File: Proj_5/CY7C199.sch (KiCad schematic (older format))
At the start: 8 parts

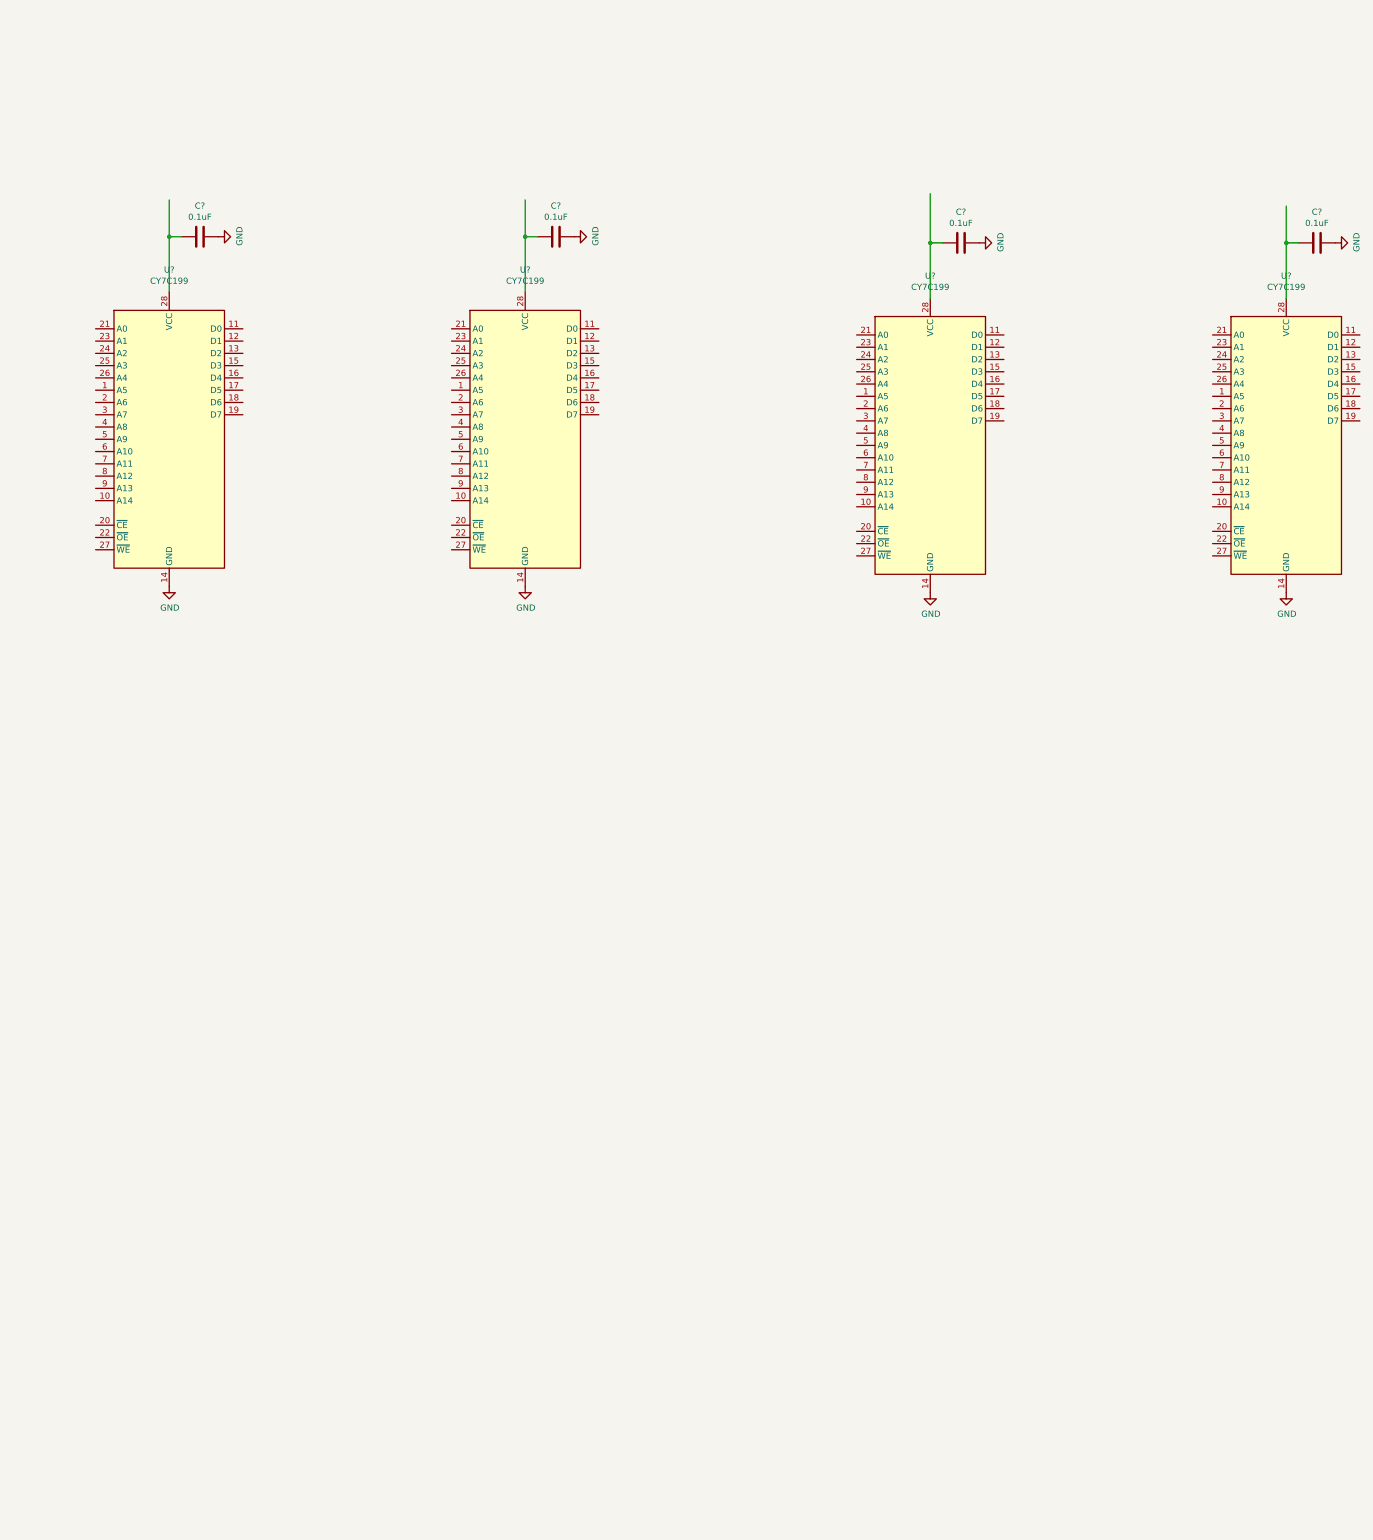
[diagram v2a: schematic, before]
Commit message: Changed Addressing Again
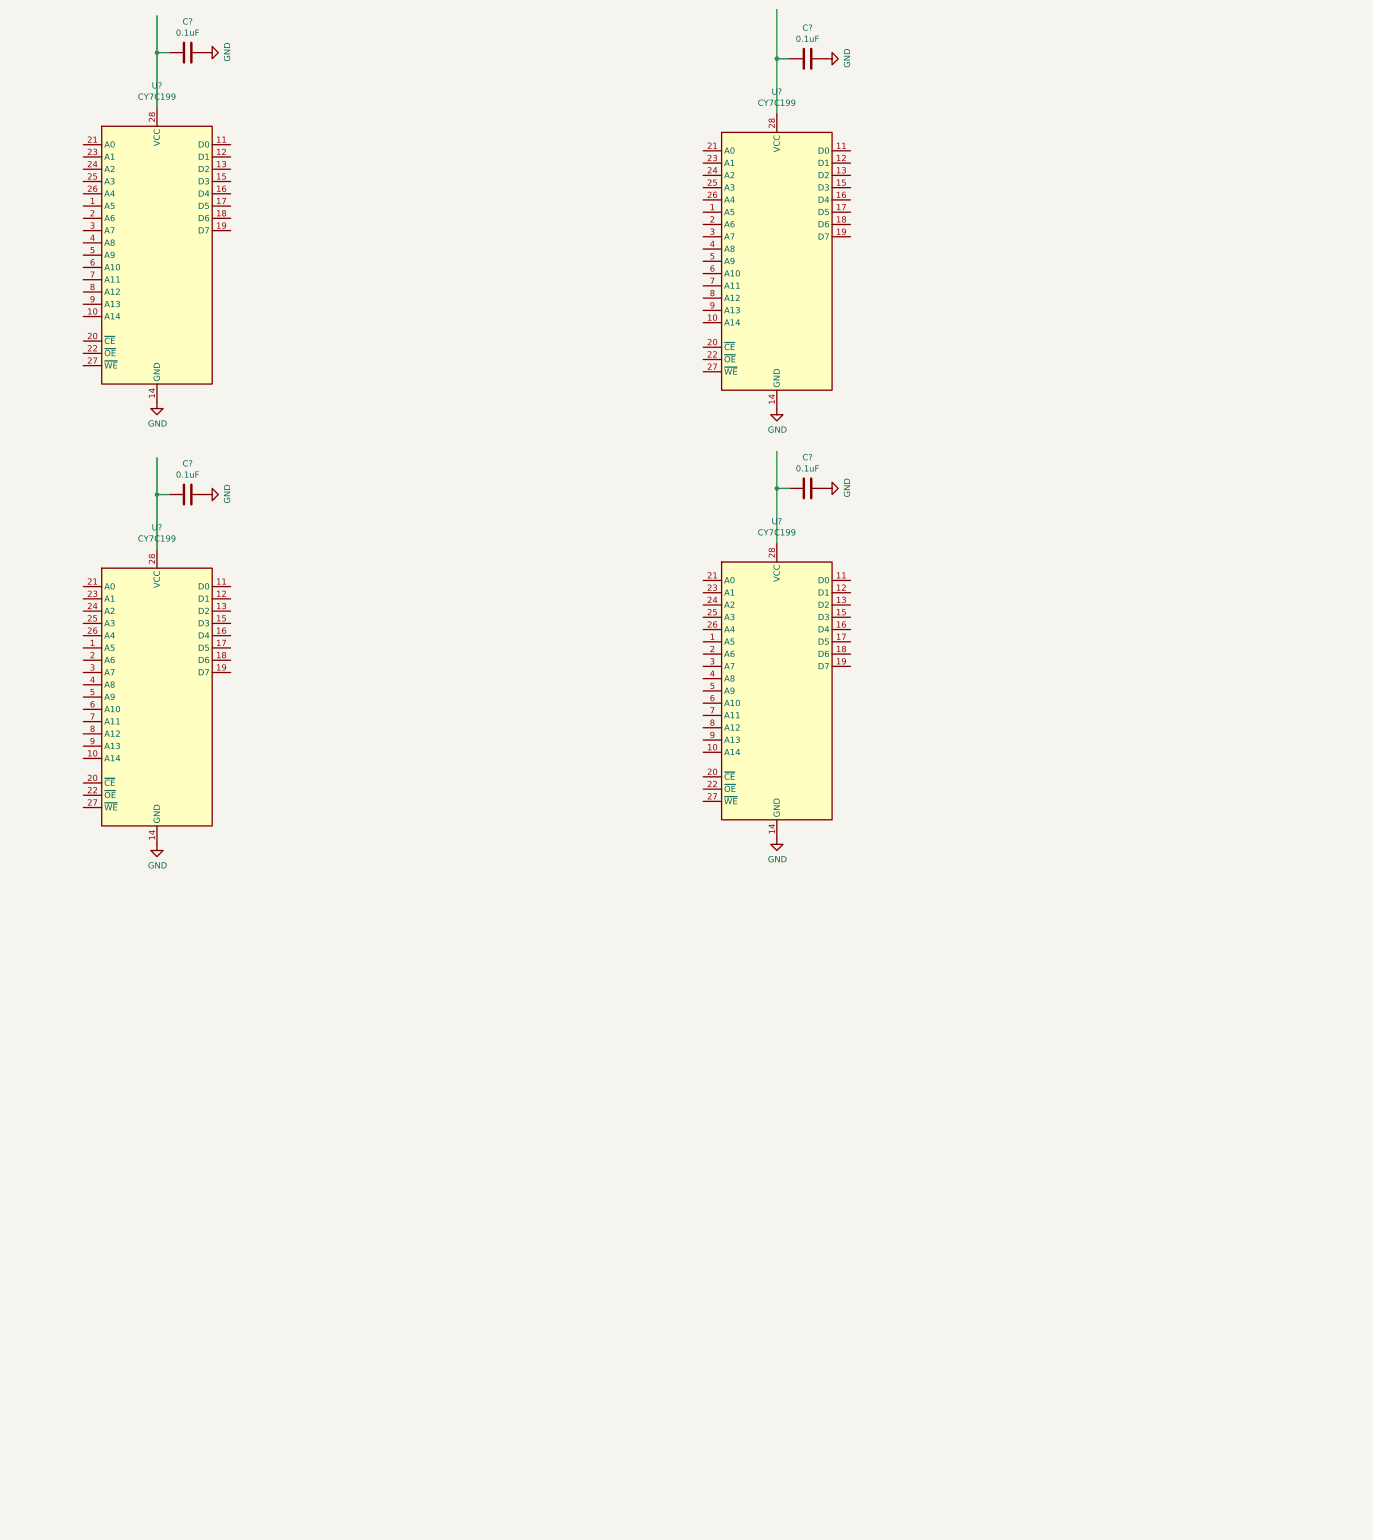
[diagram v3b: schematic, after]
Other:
- moved on the sheet: C?, U?
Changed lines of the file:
@@
 L Memory_RAM:CY7C199 U?
 U 1 1 5EA4313E
-P 4650 4500
-F 0 "U?" H 4650 5881 50  0000 C CNN
-F 1 "CY7C199" H 4650 5790 50  0000 C CNN
-F 2 "" H 4650 4500 50  0001 C CNN
-F 3 "" H 4650 4500 50  0001 C CNN
-	1    4650 4500
+P 4550 3000
+F 0 "U?" H 4550 4381 50  0000 C CNN
+F 1 "CY7C199" H 4550 4290 50  0000 C CNN
+F 2 "" H 4550 3000 50  0001 C CNN
+F 3 "" H 4550 3000 50  0001 C CNN
+	1    4550 3000
 	1    0    0    -1
 $EndComp
@@
 L Memory_RAM:CY7C199 U?
 U 1 1 5EA4B54C
-P 7550 4500
-F 0 "U?" H 7550 5881 50  0000 C CNN
-F 1 "CY7C199" H 7550 5790 50  0000 C CNN
-F 2 "" H 7550 4500 50  0001 C CNN
-F 3 "" H 7550 4500 50  0001 C CNN
-	1    7550 4500
+P 4550 6600
+F 0 "U?" H 4550 7981 50  0000 C CNN
+F 1 "CY7C199" H 4550 7890 50  0000 C CNN
+F 2 "" H 4550 6600 50  0001 C CNN
+F 3 "" H 4550 6600 50  0001 C CNN
+	1    4550 6600
 	1    0    0    -1
 $EndComp
@@
 L Memory_RAM:CY7C199 U?
 U 1 1 5EA4FA2E
-P 10850 4550
-F 0 "U?" H 10850 5931 50  0000 C CNN
-F 1 "CY7C199" H 10850 5840 50  0000 C CNN
-F 2 "" H 10850 4550 50  0001 C CNN
-F 3 "" H 10850 4550 50  0001 C CNN
-	1    10850 4550
+P 9600 3050
+F 0 "U?" H 9600 4431 50  0000 C CNN
+F 1 "CY7C199" H 9600 4340 50  0000 C CNN
+F 2 "" H 9600 3050 50  0001 C CNN
+F 3 "" H 9600 3050 50  0001 C CNN
+	1    9600 3050
 	1    0    0    -1
 $EndComp
@@
 L Memory_RAM:CY7C199 U?
 U 1 1 5EA4FA34
-P 13750 4550
-F 0 "U?" H 13750 5931 50  0000 C CNN
-F 1 "CY7C199" H 13750 5840 50  0000 C CNN
-F 2 "" H 13750 4550 50  0001 C CNN
-F 3 "" H 13750 4550 50  0001 C CNN
-	1    13750 4550
+P 9600 6550
+F 0 "U?" H 9600 7931 50  0000 C CNN
+F 1 "CY7C199" H 9600 7840 50  0000 C CNN
+F 2 "" H 9600 6550 50  0001 C CNN
+F 3 "" H 9600 6550 50  0001 C CNN
+	1    9600 6550
 	1    0    0    -1
 $EndComp
@@
 L Device:C C?
 U 1 1 5EA524F8
-P 14000 2900
-F 0 "C?" V 13748 2900 50  0000 C CNN
-F 1 "0.1uF" V 13839 2900 50  0000 C CNN
-F 2 "" H 14038 2750 50  0001 C CNN
-F 3 "~" H 14000 2900 50  0001 C CNN
-	1    14000 2900
+P 9850 4900
+F 0 "C?" V 9598 4900 50  0000 C CNN
+F 1 "0.1uF" V 9689 4900 50  0000 C CNN
+F 2 "" H 9888 4750 50  0001 C CNN
+F 3 "~" H 9850 4900 50  0001 C CNN
+	1    9850 4900
 	0    1    1    0
 $EndComp
@@
 L Device:C C?
 U 1 1 5EA53D82
-P 11100 2900
-F 0 "C?" V 10848 2900 50  0000 C CNN
-F 1 "0.1uF" V 10939 2900 50  0000 C CNN
-F 2 "" H 11138 2750 50  0001 C CNN
-F 3 "~" H 11100 2900 50  0001 C CNN
-	1    11100 2900
-	0    1    1    0
-$EndComp
-Wire Wire Line
-	13850 2900 13750 2900
-Wire Wire Line
-	13750 2900 13750 3350
-Wire Wire Line
-	13750 2900 13750 2600
-Connection ~ 13750 2900
+P 9850 1400
+F 0 "C?" V 9598 1400 50  0000 C CNN
+F 1 "0.1uF" V 9689 1400 50  0000 C CNN
+F 2 "" H 9888 1250 50  0001 C CNN
+F 3 "~" H 9850 1400 50  0001 C CNN
+	1    9850 1400
+	0    1    1    0
+$EndComp
+Wire Wire Line
+	9700 4900 9600 4900
+Wire Wire Line
+	9600 4900 9600 5350
+Wire Wire Line
+	9600 4900 9600 4600
+Connection ~ 9600 4900
 $Comp
 L power:GND #PWR?
 U 1 1 5EAA219F
-P 14150 2900
+P 10000 4900
 AR Path="/5E9F3A3D/5EAA219F" Ref="#PWR?"  Part="1"
 AR Path="/5EA98353/5EAA219F" Ref="#PWR?"  Part="1"
-F 0 "#PWR?" H 14150 2650 50  0001 C CNN
-F 1 "GND" H 14155 2727 50  0000 C CNN
-F 2 "" H 14150 2900 50  0001 C CNN
-F 3 "" H 14150 2900 50  0001 C CNN
-	1    14150 2900
+F 0 "#PWR?" H 10000 4650 50  0001 C CNN
+F 1 "GND" H 10005 4727 50  0000 C CNN
+F 2 "" H 10000 4900 50  0001 C CNN
+F 3 "" H 10000 4900 50  0001 C CNN
+	1    10000 4900
 	0    -1   -1   0
 $EndComp
@@
 L power:GND #PWR?
 U 1 1 5EAA2618
-P 11250 2900
+P 10000 1400
 AR Path="/5E9F3A3D/5EAA2618" Ref="#PWR?"  Part="1"
 AR Path="/5EA98353/5EAA2618" Ref="#PWR?"  Part="1"
-F 0 "#PWR?" H 11250 2650 50  0001 C CNN
-F 1 "GND" H 11255 2727 50  0000 C CNN
-F 2 "" H 11250 2900 50  0001 C CNN
-F 3 "" H 11250 2900 50  0001 C CNN
-	1    11250 2900
-	0    -1   -1   0
-$EndComp
-Wire Wire Line
-	10950 2900 10850 2900
-Wire Wire Line
-	10850 2900 10850 3350
+F 0 "#PWR?" H 10000 1150 50  0001 C CNN
+F 1 "GND" H 10005 1227 50  0000 C CNN
+F 2 "" H 10000 1400 50  0001 C CNN
+F 3 "" H 10000 1400 50  0001 C CNN
+	1    10000 1400
+	0    -1   -1   0
+$EndComp
+Wire Wire Line
+	9700 1400 9600 1400
+Wire Wire Line
+	9600 1400 9600 1850
 $Comp
 L Device:C C?
 U 1 1 5EAB250B
-P 7800 2850
-F 0 "C?" V 7548 2850 50  0000 C CNN
-F 1 "0.1uF" V 7639 2850 50  0000 C CNN
-F 2 "" H 7838 2700 50  0001 C CNN
-F 3 "~" H 7800 2850 50  0001 C CNN
-	1    7800 2850
-	0    1    1    0
-$EndComp
-Wire Wire Line
-	7650 2850 7550 2850
-Wire Wire Line
-	7550 2850 7550 3300
-Wire Wire Line
-	7550 2850 7550 2550
-Connection ~ 7550 2850
+P 4800 4950
+F 0 "C?" V 4548 4950 50  0000 C CNN
+F 1 "0.1uF" V 4639 4950 50  0000 C CNN
+F 2 "" H 4838 4800 50  0001 C CNN
+F 3 "~" H 4800 4950 50  0001 C CNN
+	1    4800 4950
+	0    1    1    0
+$EndComp
+Wire Wire Line
+	4650 4950 4550 4950
+Wire Wire Line
+	4550 4950 4550 5400
+Wire Wire Line
+	4550 4950 4550 4650
+Connection ~ 4550 4950
 $Comp
 L power:GND #PWR?
 U 1 1 5EAB2515
-P 7950 2850
+P 4950 4950
 AR Path="/5E9F3A3D/5EAB2515" Ref="#PWR?"  Part="1"
 AR Path="/5EA98353/5EAB2515" Ref="#PWR?"  Part="1"
-F 0 "#PWR?" H 7950 2600 50  0001 C CNN
-F 1 "GND" H 7955 2677 50  0000 C CNN
-F 2 "" H 7950 2850 50  0001 C CNN
-F 3 "" H 7950 2850 50  0001 C CNN
-	1    7950 2850
+F 0 "#PWR?" H 4950 4700 50  0001 C CNN
+F 1 "GND" H 4955 4777 50  0000 C CNN
+F 2 "" H 4950 4950 50  0001 C CNN
+F 3 "" H 4950 4950 50  0001 C CNN
+	1    4950 4950
 	0    -1   -1   0
 $EndComp
@@
 L Device:C C?
 U 1 1 5EAB3F01
-P 4900 2850
-F 0 "C?" V 4648 2850 50  0000 C CNN
-F 1 "0.1uF" V 4739 2850 50  0000 C CNN
-F 2 "" H 4938 2700 50  0001 C CNN
-F 3 "~" H 4900 2850 50  0001 C CNN
-	1    4900 2850
-	0    1    1    0
-$EndComp
-Wire Wire Line
-	4750 2850 4650 2850
-Wire Wire Line
-	4650 2850 4650 3300
-Wire Wire Line
-	4650 2850 4650 2550
-Connection ~ 4650 2850
+P 4800 1350
+F 0 "C?" V 4548 1350 50  0000 C CNN
+F 1 "0.1uF" V 4639 1350 50  0000 C CNN
+F 2 "" H 4838 1200 50  0001 C CNN
+F 3 "~" H 4800 1350 50  0001 C CNN
+	1    4800 1350
+	0    1    1    0
+$EndComp
+Wire Wire Line
+	4650 1350 4550 1350
+Wire Wire Line
+	4550 1350 4550 1800
+Wire Wire Line
+	4550 1350 4550 1050
+Connection ~ 4550 1350
 $Comp
 L power:GND #PWR?
 U 1 1 5EAB3F0B
-P 5050 2850
+P 4950 1350
 AR Path="/5E9F3A3D/5EAB3F0B" Ref="#PWR?"  Part="1"
 AR Path="/5EA98353/5EAB3F0B" Ref="#PWR?"  Part="1"
-F 0 "#PWR?" H 5050 2600 50  0001 C CNN
-F 1 "GND" H 5055 2677 50  0000 C CNN
-F 2 "" H 5050 2850 50  0001 C CNN
-F 3 "" H 5050 2850 50  0001 C CNN
-	1    5050 2850
-	0    -1   -1   0
-$EndComp
-Wire Wire Line
-	10850 2900 10850 2500
-Connection ~ 10850 2900
+F 0 "#PWR?" H 4950 1100 50  0001 C CNN
+F 1 "GND" H 4955 1177 50  0000 C CNN
+F 2 "" H 4950 1350 50  0001 C CNN
+F 3 "" H 4950 1350 50  0001 C CNN
+	1    4950 1350
+	0    -1   -1   0
+$EndComp
+Wire Wire Line
+	9600 1400 9600 1000
+Connection ~ 9600 1400
 $Comp
 L power:GND #PWR?
 U 1 1 5EAB5C11
-P 10850 5750
+P 9600 4250
 AR Path="/5E9F3A3D/5EAB5C11" Ref="#PWR?"  Part="1"
 AR Path="/5EA98353/5EAB5C11" Ref="#PWR?"  Part="1"
-F 0 "#PWR?" H 10850 5500 50  0001 C CNN
-F 1 "GND" H 10855 5577 50  0000 C CNN
-F 2 "" H 10850 5750 50  0001 C CNN
-F 3 "" H 10850 5750 50  0001 C CNN
-	1    10850 5750
+F 0 "#PWR?" H 9600 4000 50  0001 C CNN
+F 1 "GND" H 9605 4077 50  0000 C CNN
+F 2 "" H 9600 4250 50  0001 C CNN
+F 3 "" H 9600 4250 50  0001 C CNN
+	1    9600 4250
 	1    0    0    -1
 $EndComp
@@
 L power:GND #PWR?
 U 1 1 5EAB5EF1
-P 13750 5750
+P 9600 7750
 AR Path="/5E9F3A3D/5EAB5EF1" Ref="#PWR?"  Part="1"
 AR Path="/5EA98353/5EAB5EF1" Ref="#PWR?"  Part="1"
-F 0 "#PWR?" H 13750 5500 50  0001 C CNN
-F 1 "GND" H 13755 5577 50  0000 C CNN
-F 2 "" H 13750 5750 50  0001 C CNN
-F 3 "" H 13750 5750 50  0001 C CNN
-	1    13750 5750
+F 0 "#PWR?" H 9600 7500 50  0001 C CNN
+F 1 "GND" H 9605 7577 50  0000 C CNN
+F 2 "" H 9600 7750 50  0001 C CNN
+F 3 "" H 9600 7750 50  0001 C CNN
+	1    9600 7750
 	1    0    0    -1
 $EndComp
@@
 L power:GND #PWR?
 U 1 1 5EAB6217
-P 7550 5700
+P 4550 7800
 AR Path="/5E9F3A3D/5EAB6217" Ref="#PWR?"  Part="1"
 AR Path="/5EA98353/5EAB6217" Ref="#PWR?"  Part="1"
-F 0 "#PWR?" H 7550 5450 50  0001 C CNN
-F 1 "GND" H 7555 5527 50  0000 C CNN
-F 2 "" H 7550 5700 50  0001 C CNN
-F 3 "" H 7550 5700 50  0001 C CNN
-	1    7550 5700
+F 0 "#PWR?" H 4550 7550 50  0001 C CNN
+F 1 "GND" H 4555 7627 50  0000 C CNN
+F 2 "" H 4550 7800 50  0001 C CNN
+F 3 "" H 4550 7800 50  0001 C CNN
+	1    4550 7800
 	1    0    0    -1
 $EndComp
@@
 L power:GND #PWR?
 U 1 1 5EAB6544
-P 4650 5700
+P 4550 4200
 AR Path="/5E9F3A3D/5EAB6544" Ref="#PWR?"  Part="1"
 AR Path="/5EA98353/5EAB6544" Ref="#PWR?"  Part="1"
-F 0 "#PWR?" H 4650 5450 50  0001 C CNN
-F 1 "GND" H 4655 5527 50  0000 C CNN
-F 2 "" H 4650 5700 50  0001 C CNN
-F 3 "" H 4650 5700 50  0001 C CNN
-	1    4650 5700
-	1    0    0    -1
-$EndComp
+F 0 "#PWR?" H 4550 3950 50  0001 C CNN
+F 1 "GND" H 4555 4027 50  0000 C CNN
+F 2 "" H 4550 4200 50  0001 C CNN
+F 3 "" H 4550 4200 50  0001 C CNN
+	1    4550 4200
+	1    0    0    -1
+$EndComp

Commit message: Dinner Break
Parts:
- added U? (x2): 74AHCT1G04, symbol 74xGxx:74AHCT1G04
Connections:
- net labels added: A0, A1, A10, A11, A12, A13, A14, A15, A16, A17, A18, A19, A2, A3, A4, A5, A6, A7, A8, A9, D0, D1, D10, D11, D12, D13, D14, D15, D2, D3, D4, D5, D6, D7, D8, D9
- wire segments 12 -> 114
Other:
- note added: "High Bank"
- note added: "Low Bank"
- moved on the sheet: C?, U?
